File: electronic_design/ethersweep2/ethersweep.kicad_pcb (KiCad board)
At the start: 2 copper layers, 79 x 38 mm, 69 parts, among them J1 AVR-ISP-6, J2 Conn_01x02_Male, J3 Conn_01x04_Female, J4 Conn_01x02_Male, J5 Conn_01x02_Male, J6 HR911105A, J7 Conn_01x06_Female, J8 AVR-ISP-6, J9 Conn_01x06_Male, M1 Stepper_Motor_bipolar, SW1 SW_Push, U1 ENC28J60x-SS, U2 ATmega328-AU, U3 DRV8825PWPR, U4 AMS1117-3.3, U5 AS5600, Y1 Crystal_25MHz, Y2 Crystal_8MHz

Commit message: design improvements and error fixes
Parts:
- C13, C14, C15, C16, C17, C3, C4, C5, C7, D1, J3, J8, R10, R13, R3, R4, R5, R6, R7, R8, R9, SW1, U1, Y1: moved to F.Cu
- H5, H6, H7, H8, J4, J5, J6, J7: moved to B.Cu
- moved D1 33.0 mm to (148.0, 83.5), turned to 270 degrees
- moved H5 31.0 mm to (126.0, 115.5)
- moved H6 31.0 mm to (157.0, 115.5)
- moved H7 31.0 mm to (157.0, 84.5)
- moved H8 31.0 mm to (126.0, 84.5)
- moved SW1 31.0 mm to (151.5, 84.5), turned to 90 degrees
- moved J4 28.0 mm to (133.0, 114.0)
- moved J5 28.0 mm to (141.0, 114.0)
- moved R13 27.0 mm to (148.0, 86.5)
- moved J8 25.0 mm to (149.0, 112.5)
- moved R3 23.0 mm to (151.5, 88.5)
- moved J7 20.2 mm to (156.6, 110.0), turned to 90 degrees
- moved C15 17.0 mm to (133.5, 108.5)
- moved R1 16.5 mm to (164.5, 93.0), turned to 90 degrees
- moved C13 15.0 mm to (129.0, 107.5), turned to 270 degrees
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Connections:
- net SLP_ETHERNET renamed Net-(U2-Pad14)
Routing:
- net ENDSTOP: track 34.8 -> 16.2 mm
- net ESTOP: track 41.7 -> 27.3 mm, vias 1 -> 0
- net CS_ETHERNET: track 39.2 -> 25.4 mm
- net RST_ETHERNET: track 39.4 -> 27.6 mm
- net SCL: track 78.7 -> 67.3 mm
- net rst: track 67.6 -> 59.8 mm
- net SCK: track 43.0 -> 37.2 mm
- net SDA: track 76.6 -> 71.1 mm, vias 6 -> 5
- net GND: track 109.2 -> 112.7 mm, vias 149 -> 134
- net +3V3: track 219.5 -> 217.8 mm, vias 13 -> 14
- net M0: track 29.2 -> 28.3 mm
- net M1: track 37.1 -> 37.8 mm
- net MISO: track 38.0 -> 38.4 mm, vias 0 -> 3
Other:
- outline, holes or cut-outs redrawn
- board text added: "VERSION: 2.0.1"
- board text added: "by Neumi 2021-02-03"

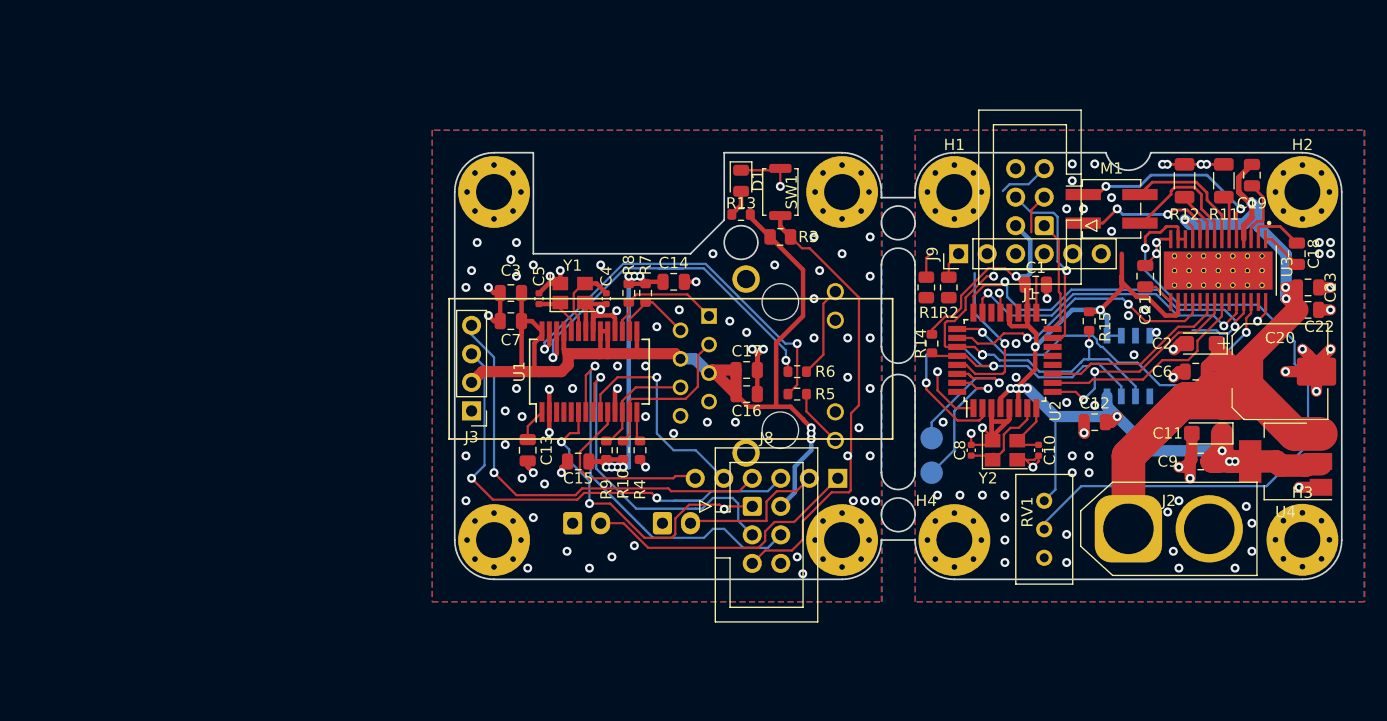
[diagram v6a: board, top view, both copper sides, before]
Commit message: changed images
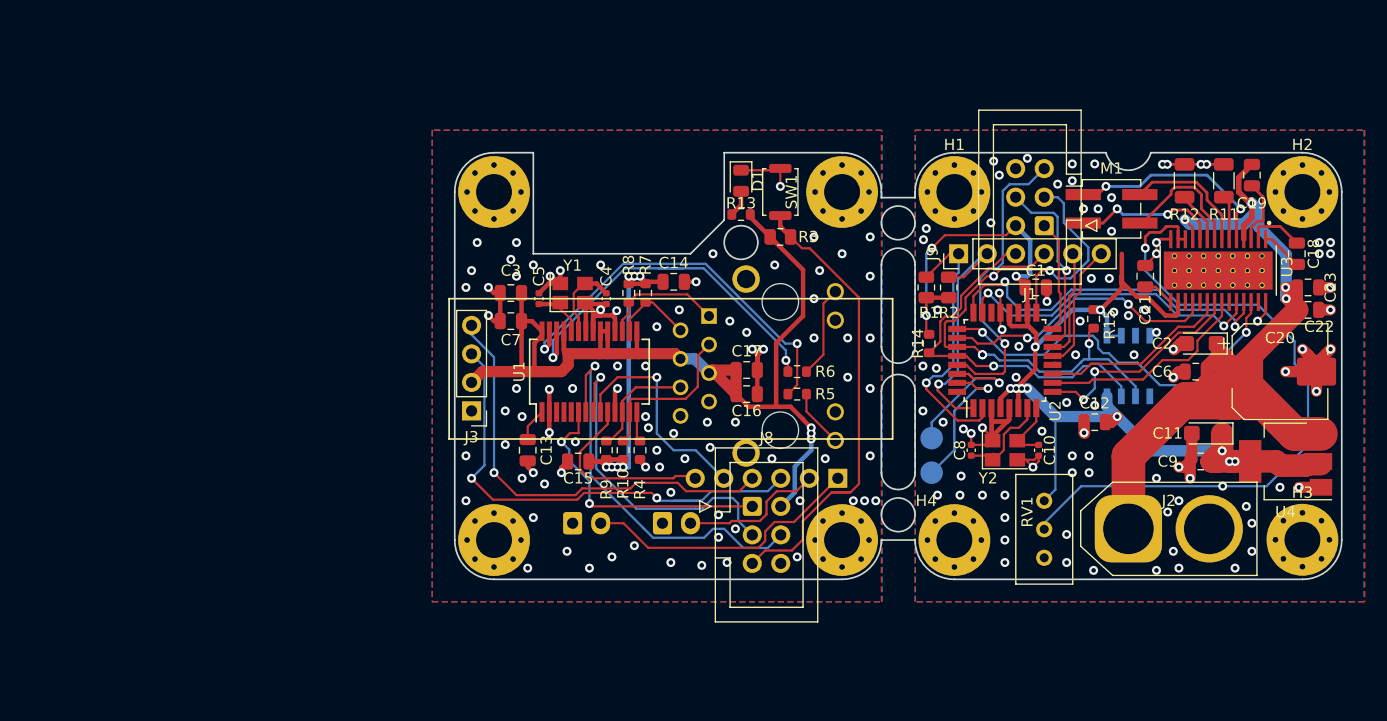
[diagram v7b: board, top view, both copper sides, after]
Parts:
- moved R15 0.45 mm to (179.4, 95.8)
- moved C1 0.25 mm to (174.2, 93.0)
- moved R14 0.25 mm to (164.8, 98.0)
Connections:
- U2 pad 1: CS_ETHERNET -> ENDSTOP
- U2 pad 12: ENDSTOP -> Net-(U2-Pad12)
- U2 pad 13: ESTOP -> RST_ETHERNET
- U2 pad 14: Net-(U2-Pad14) -> CS_ETHERNET
- U2 pad 2: RST_ETHERNET -> ESTOP
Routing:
- net ESTOP: track 27.3 -> 50.2 mm, vias 0 -> 1
- net ENDSTOP: track 16.2 -> 36.2 mm, vias 0 -> 1
- net SCL: track 67.3 -> 77.5 mm
- net SCK: track 37.2 -> 47.3 mm, vias 1 -> 2
- net rst: track 59.8 -> 69.5 mm, vias 2 -> 1
- net +3V3: track 217.8 -> 226.7 mm, vias 14 -> 16
- net SDA: track 71.1 -> 77.2 mm
- net CS_ETHERNET: track 25.4 -> 29.6 mm, vias 2 -> 1
- net M1: track 37.8 -> 33.6 mm
- net MISO: track 38.4 -> 35.0 mm, vias 3 -> 2
- net GND: track 112.7 -> 114.0 mm, vias 134 -> 172
- net RST_ETHERNET: track 27.6 -> 28.3 mm, vias 1 -> 0
- net Net-(RV1-Pad2): vias 1 -> 2

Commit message: added prod files
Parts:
- R1, R2: value R5k -> R10k; footprint Resistor_SMD:R_0805_2012Metric -> Resistor_SMD:R_0603_1608Metric
- R3: footprint Resistor_SMD:R_0805_2012Metric -> Resistor_SMD:R_0603_1608Metric
- moved R1 0.36 mm to (164.8, 93.2)
- moved R2 0.36 mm to (166.8, 93.2)
- moved R3 0.12 mm to (151.6, 88.6)
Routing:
- net Net-(RV1-Pad2): track 60.6 -> 60.3 mm, vias 2 -> 1
- net GND: vias 172 -> 177
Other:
- board text added: "by Neumi 2021-02-05"
- board text removed: "by Neumi 2021-02-03"
